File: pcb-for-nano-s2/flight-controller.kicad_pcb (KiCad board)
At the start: 4 copper layers, 24 x 33 mm, 53 parts, among them J1 BM03B-SRSS-TBLFSN, J2 BM03B-SRSS-TBLFSN, J3 BM03B-SRSS-TBLFSN, J4 Conn_01x02, J5 Conn_ARM_JTAG_SWD_10, J6 Conn_01x02, Q1 Q_NMOS_GSD, Q2 Q_NMOS_GSD, U1 STM32G4A1KEU6, U2 ZOE-M8Q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

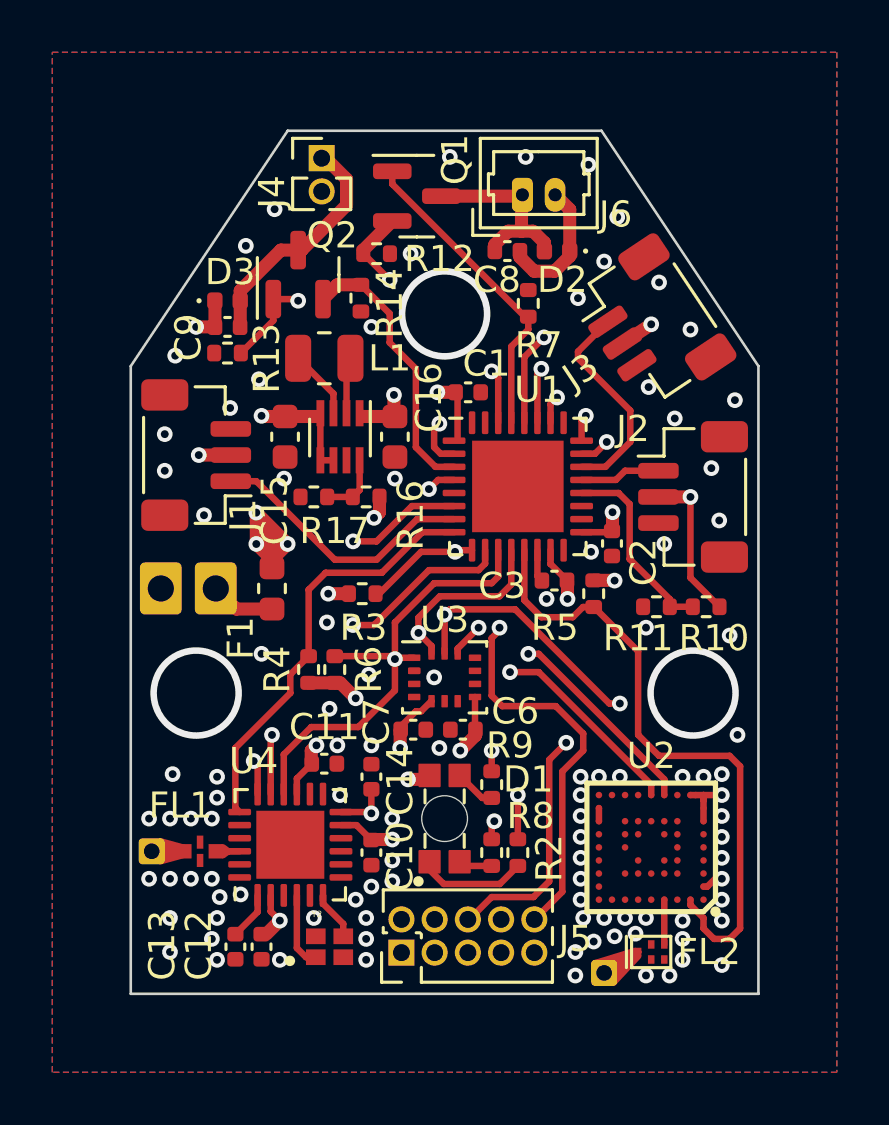
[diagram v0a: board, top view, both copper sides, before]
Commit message: add impedance matching circuits for antennas
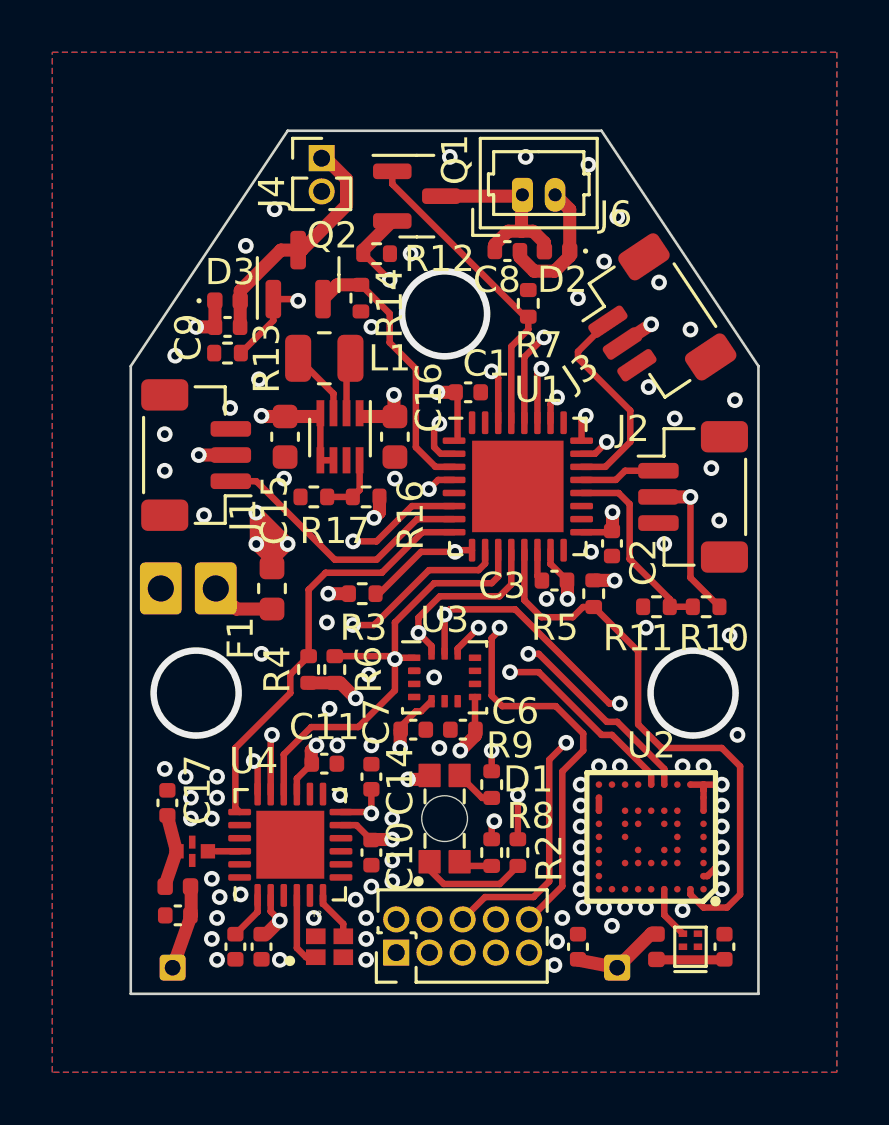
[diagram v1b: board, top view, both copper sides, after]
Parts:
- added C17: ~, Capacitor_SMD:C_0402_1005Metric, F.Cu at (139.4, 105.7)
- added C18: ~, Capacitor_SMD:C_0402_1005Metric, F.Cu at (139.8, 110.0)
- added C4: ~, Capacitor_SMD:C_0402_1005Metric, F.Cu at (155.1, 111.2)
- added C5: ~, Capacitor_SMD:C_0402_1005Metric, F.Cu at (160.7, 111.2)
- added L2: ~, Inductor_SMD:L_0402_1005Metric, F.Cu at (158.1, 111.2)
- added L3: ~, Inductor_SMD:L_0402_1005Metric, F.Cu at (139.8, 108.9)
- moved RADIO1 4.52 mm to (139.6, 112.0)
- moved FL2 1.51 mm to (159.4, 111.2), turned to 90 degrees
- moved GNSS1 0.54 mm to (156.6, 112.0)
- moved U2 0.40 mm to (157.9, 107.0)
- moved FL1 0.30 mm to (140.3, 107.5)
- moved J5 0.20 mm to (148.2, 111.4)
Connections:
- FL1 pad 3: Net-(FL1-Pad3) -> Net-(C17-Pad2)
- FL2 pad 1: Net-(FL2-Pad1) -> Net-(C5-Pad2)
- GNSS1 pad 1: Net-(FL2-Pad1) -> Net-(C4-Pad2)
- RADIO1 pad 1: Net-(FL1-Pad3) -> Net-(C18-Pad2)
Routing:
- net Net-(FL2-Pad1): track 6.45 -> 0.00 mm
- net Net-(C4-Pad2): track 0.00 -> 3.57 mm
- net Net-(C18-Pad2): track 0.00 -> 3.22 mm
- net Net-(C17-Pad2): track 0.00 -> 2.81 mm
- net Net-(C5-Pad2): track 0.00 -> 2.58 mm
- net /~{GNSS_CS}: track 24.2 -> 22.2 mm
- net Net-(FL1-Pad3): track 1.89 -> 0.00 mm
- net /SCK: track 39.4 -> 38.8 mm
- net GND: vias 103 -> 89

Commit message: remove solder mask expansion
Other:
- rule pad_to_mask_clearance: 0.025 -> 0
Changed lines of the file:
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@@
       (dielectric_constraints no)
     )
-    (pad_to_mask_clearance 0.025)
+    (pad_to_mask_clearance 0)
     (pcbplotparams
       (layerselection 0x00010fc_ffffffff)
